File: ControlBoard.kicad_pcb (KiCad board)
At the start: 2 copper layers, 80 x 60 mm, 99 parts, among them J1 Conn_02x07_Odd_Even, J2 Conn_02x07_Odd_Even, J3 USB_C_Receptacle_PowerOnly_6P, J4 Conn_02x05_Odd_Even, J6 Conn_01x02_MountingPin, SW1 SW_Push, SW2 SW_Push, U1 STM32G473RCTx, U2 AT24CS02-XHM, U3 ICM-42668-P, U4 RT9013-33GB, U6 TLE9251VSJ, Y1 32MHz

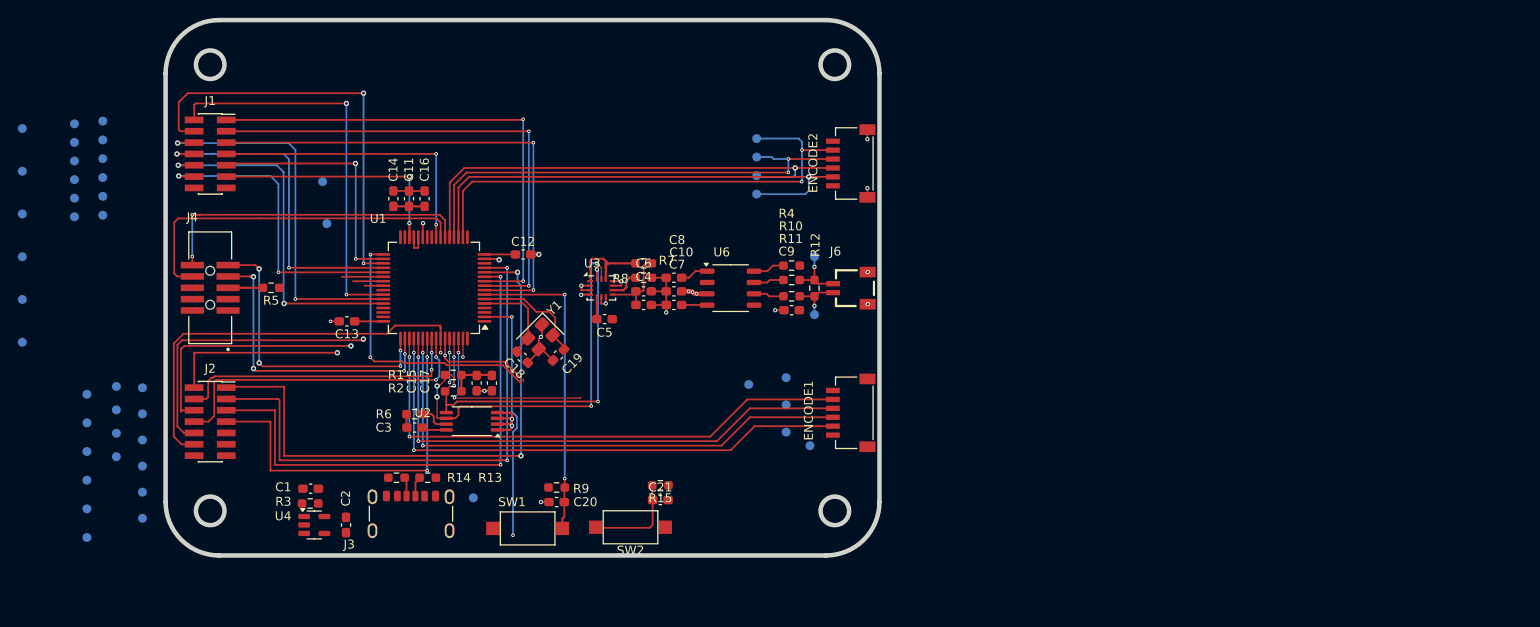
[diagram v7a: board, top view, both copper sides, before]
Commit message: 信号线布线完成
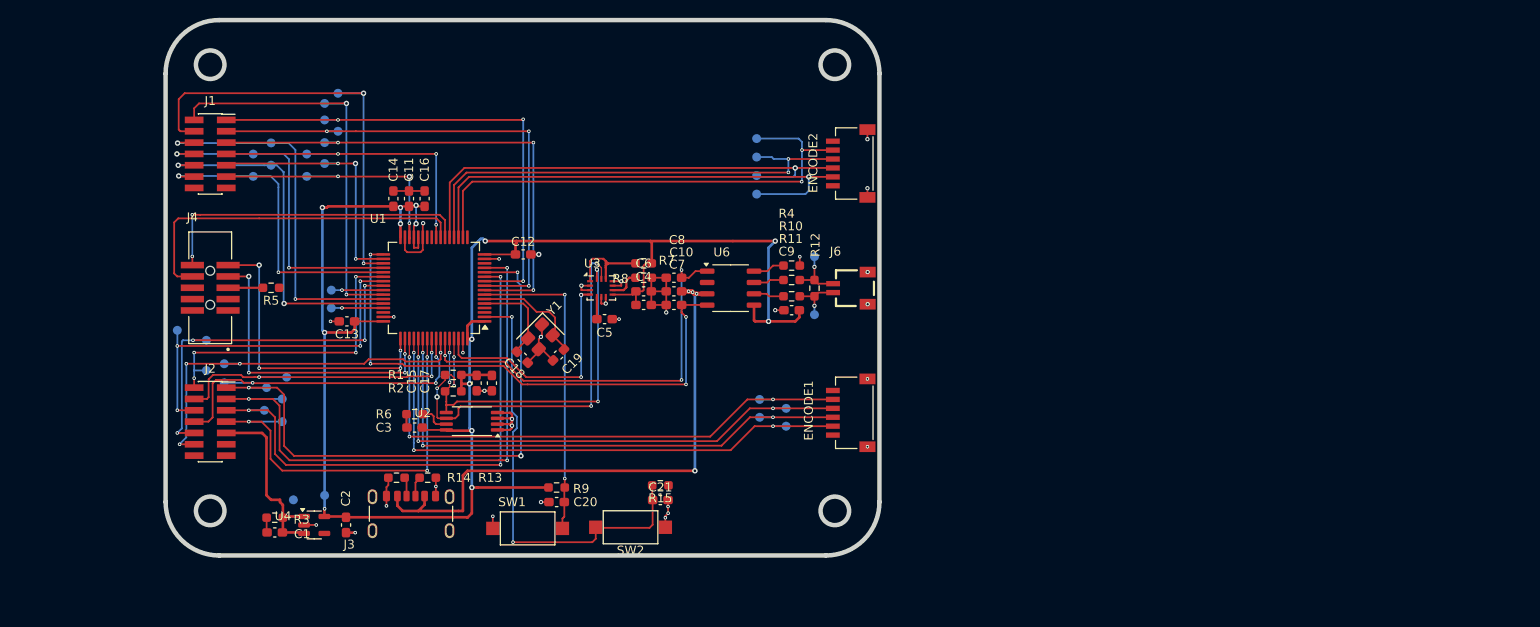
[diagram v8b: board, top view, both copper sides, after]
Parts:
- removed TP13, TP14, TP15, TP16, TP17, TP18, TP31, TP32, TP33, TP34, TP35, TP36: TestPoint_Small, TestPoint:TestPoint_Pad_D1.0mm
- moved TP48 49.1 mm to (85.8, 105.3)
- moved TP26 39.8 mm to (87.3, 60.2)
- moved TP25 36.1 mm to (85.8, 61.3)
- moved TP28 33.4 mm to (77.8, 67.0)
- moved TP27 32.9 mm to (79.8, 65.8)
- moved TP29 28.2 mm to (79.8, 68.3)
- moved TP20 28.0 mm to (87.3, 64.5)
- moved TP30 25.9 mm to (77.8, 69.5)
- moved TP19 25.7 mm to (85.8, 63.2)
- moved TP21 25.0 mm to (85.8, 65.7)
- moved TP23 24.9 mm to (85.8, 68.1)
- moved TP24 23.0 mm to (83.8, 69.5)
- moved TP22 22.9 mm to (83.8, 67.0)
- moved TP43 21.4 mm to (69.3, 86.8)
- moved TP47 20.2 mm to (82.3, 105.8)
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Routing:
- net +3.3V: track 32.6 -> 205.7 mm, vias 0 -> 14
- net +5V: track 2.98 -> 85.4 mm, vias 3 -> 4
- net /MCU_Part/Peripheral/PB6_FDCAN2_TX: track 15.2 -> 46.2 mm, vias 1 -> 3
- net /MCU_Part/Peripheral/PB11_FDCAN2_RX: track 34.0 -> 62.0 mm, vias 2 -> 4
- net GND: track 50.4 -> 74.7 mm, vias 19 -> 32
- net Net-(U1-PC13): track 39.0 -> 50.5 mm
- net /MOTOR2_U+: track 24.6 -> 34.9 mm, vias 1 -> 4
- net /MOTOR2_V+: track 31.3 -> 41.1 mm, vias 1 -> 4
- net /MOTOR2_W+: track 34.5 -> 42.7 mm, vias 1 -> 4
- net /MCU_Part/PC9_TIM8_CH4: track 0.00 -> 5.83 mm, vias 0 -> 1
- net /MCU_Part/PA11_TIM1_CH4: track 0.00 -> 5.83 mm, vias 0 -> 1
- net /MCU_Part/Peripheral/ICM-20602-INT: track 22.1 -> 26.9 mm, vias 3 -> 2
- net /MOTOR2_V-: track 36.2 -> 40.0 mm, vias 2 -> 3
- net /BusVoltage: track 32.9 -> 36.4 mm, vias 2 -> 3
- net /MOTOR1_BREAK: track 27.9 -> 31.4 mm, vias 2 -> 3
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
